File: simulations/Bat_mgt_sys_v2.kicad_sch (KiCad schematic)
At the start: 41 parts, among them Q1 PMOS, Q2 PMOS, U1 TLV76701DRVx, U2 MCP6561-OT, U4 74AHC1G02, U5 MCP6561-OT

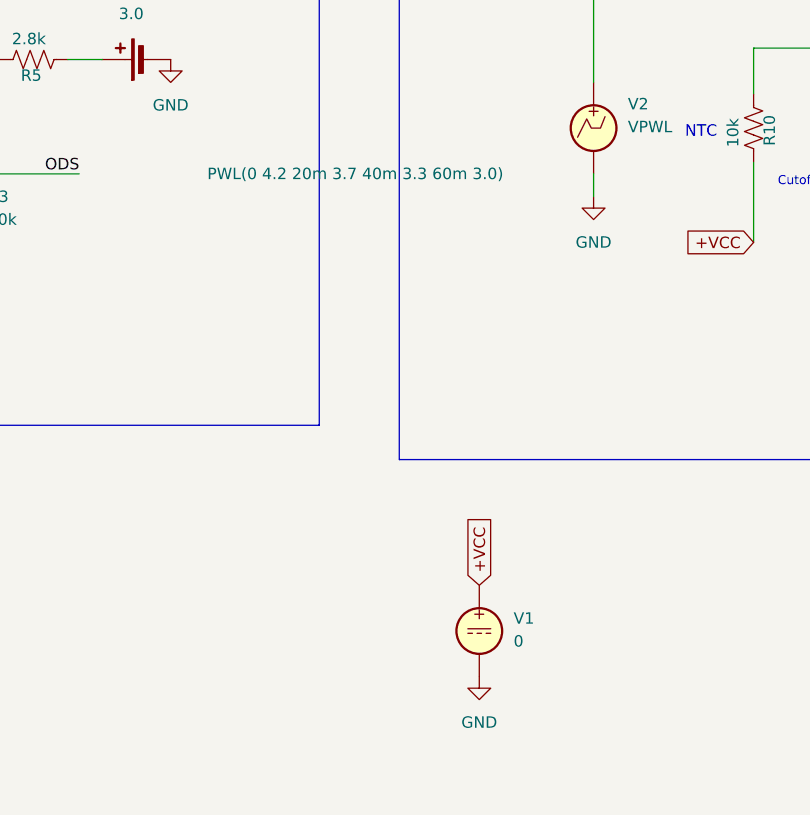
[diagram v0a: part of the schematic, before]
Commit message: added ldo diagram
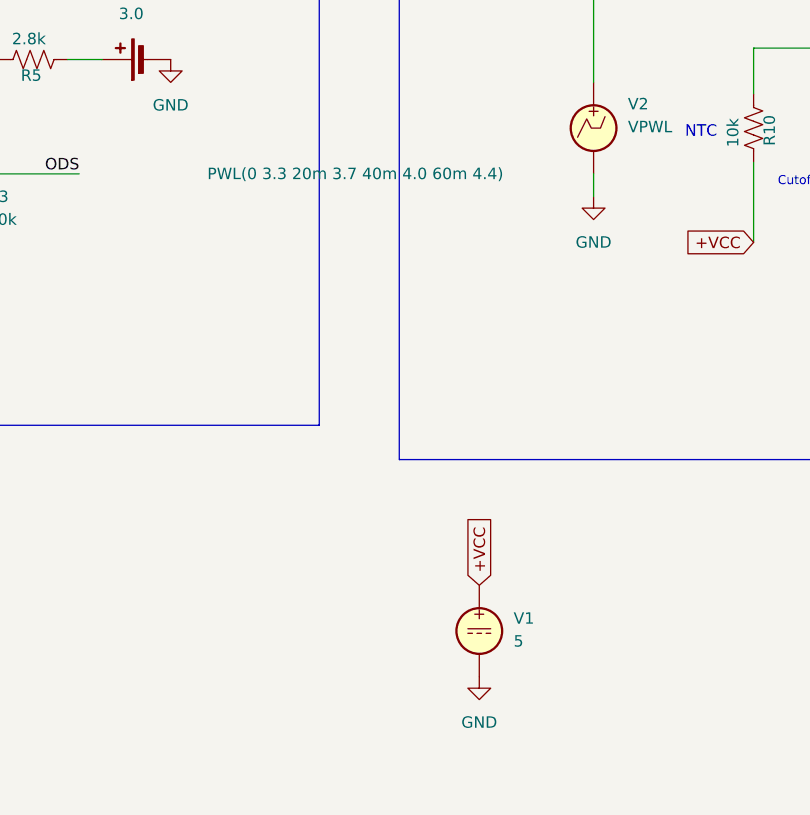
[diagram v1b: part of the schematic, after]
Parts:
- V1: value 0 -> 5
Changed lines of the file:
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@@
 			)
 		)
-		(property "Sim.Params" "PWL(0 4.2 20m 3.7 40m 3.3 60m 3.0)"
+		(property "Sim.Params" "PWL(0 3.3 20m 3.7 40m 4.0 60m 4.4)"
 			(at 169.164 176.53 0)
 			(show_name no)
@@
 			)
 		)
-		(property "Value" "0"
+		(property "Value" "5"
 			(at 203.2 228.4701 0)
 			(show_name no)
